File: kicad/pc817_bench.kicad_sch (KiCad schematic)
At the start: 14 parts, among them J1 24V inputs, J2 Arduino UNO R4, U1 PC817, U2 PC817

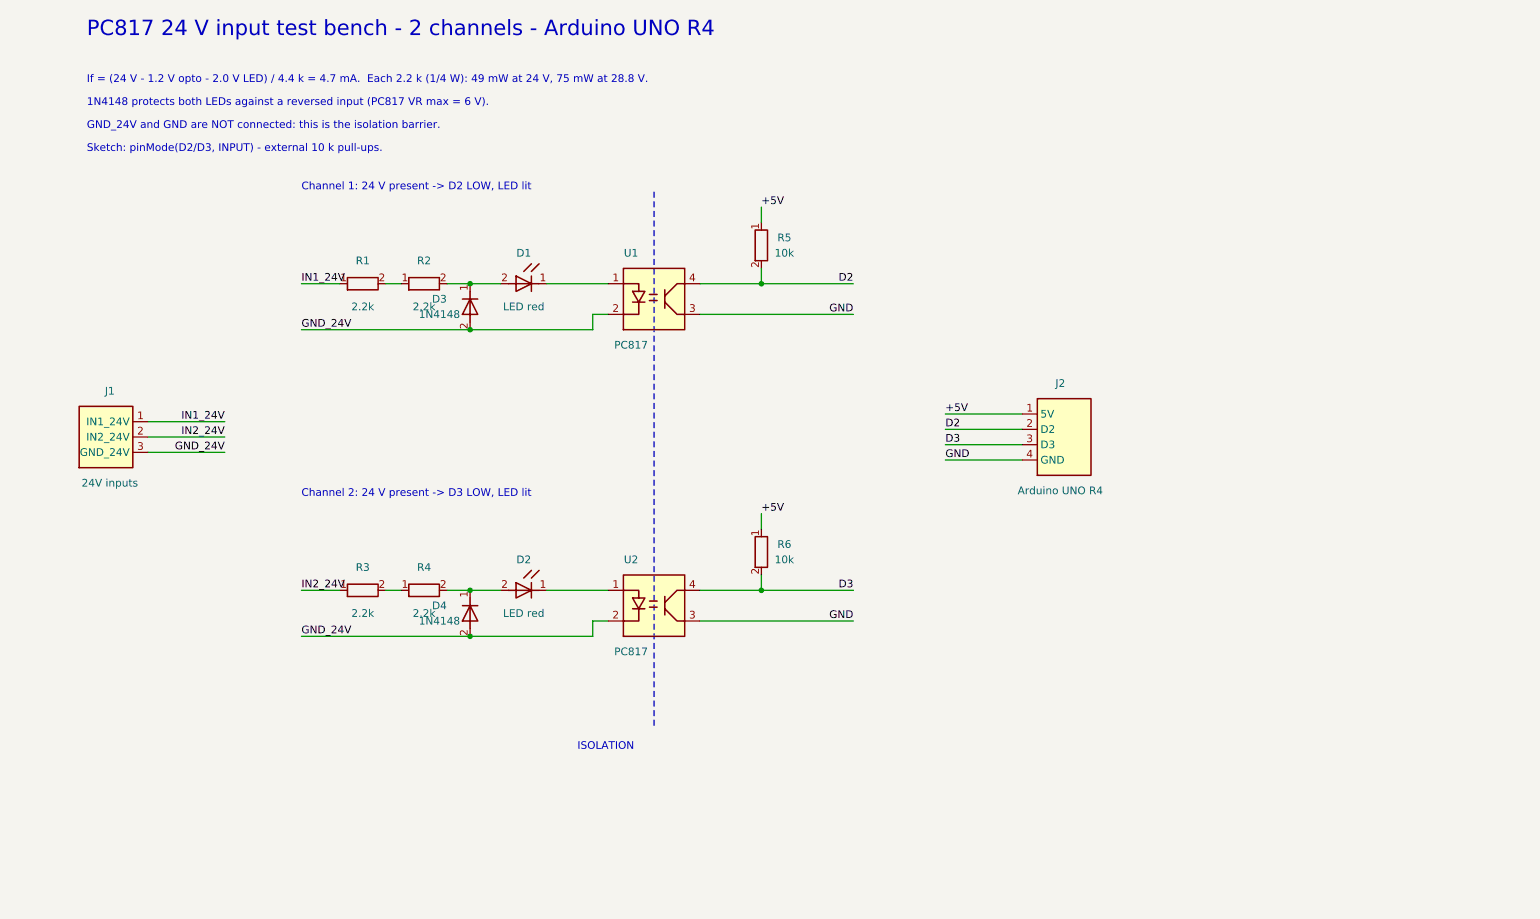
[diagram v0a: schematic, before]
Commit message: Draw the Arduino UNO R4 WiFi as a full header symbol instead of a 4-pin connector
Unused pins carry no-connect marks; all three GND pins join the GND net.
Rule check: 0 violations (KiCad 10.0.6).

Co-Authored-By: Claude Fable 5.1 <noreply@anthropic.com>
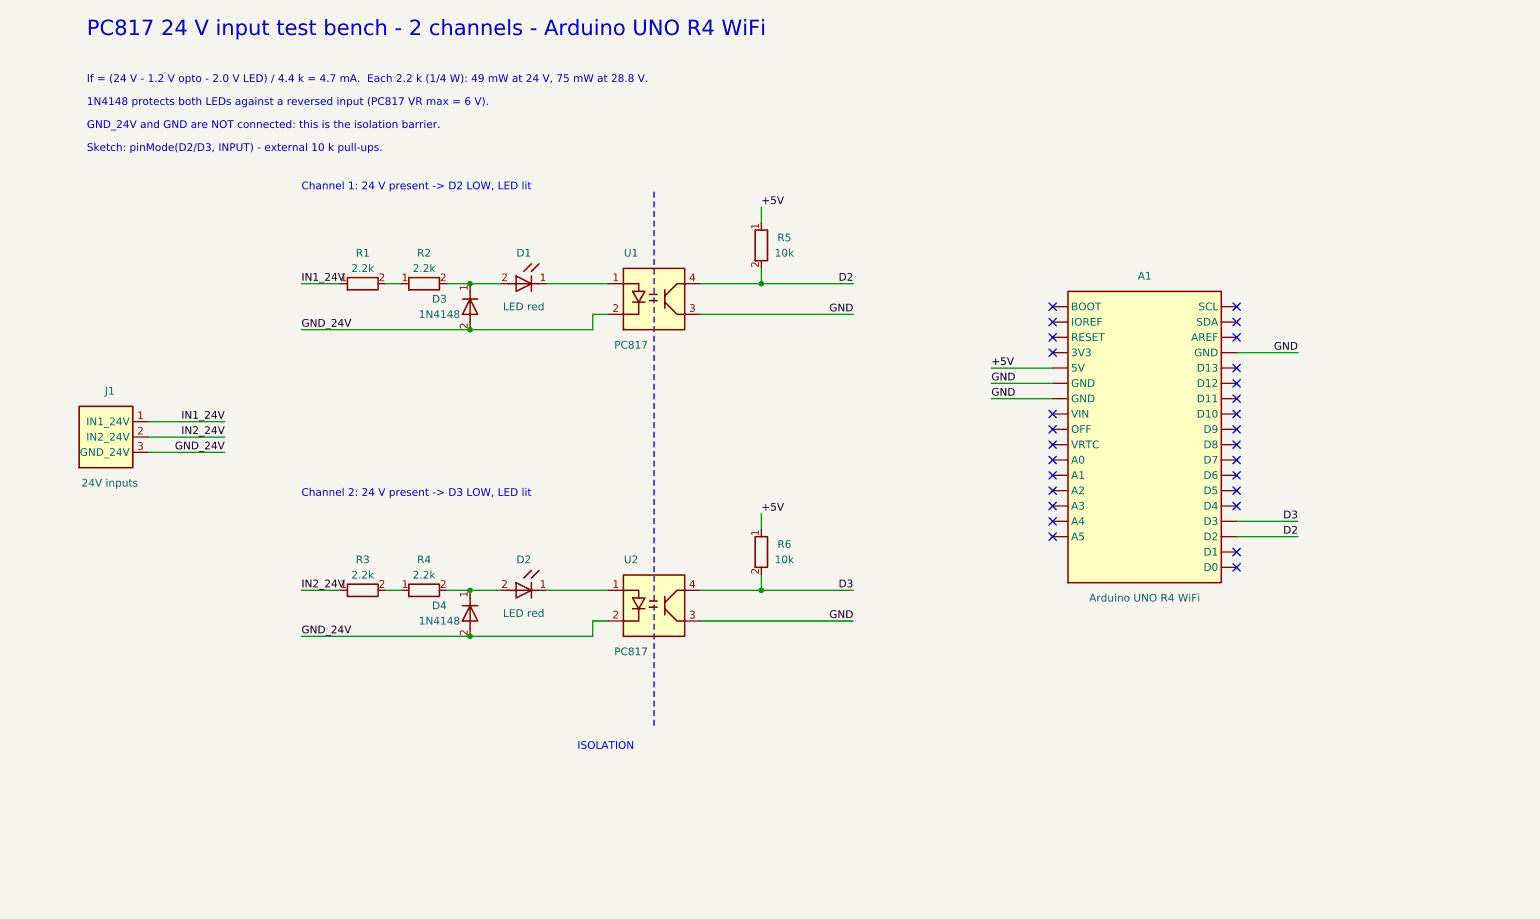
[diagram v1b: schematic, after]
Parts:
- removed J2: Arduino UNO R4, symbol bench:CONN4
- added A1: Arduino UNO R4 WiFi, symbol bench:UNO_R4_WIFI
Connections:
- net +5V: now also A1.5V
- net D2: now also A1.D2
- net D3: now also A1.D3
- net GND: now also A1.GND1 (GND), A1.GND2 (GND), A1.GND3 (GND)
- no-connect marks 0 -> 28
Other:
- note added: "PC817 24 V input test bench - 2 channels - Arduino UNO R4 WiFi"
- note removed: "PC817 24 V input test bench - 2 channels - Arduino UNO R4"
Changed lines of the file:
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@@
 (kicad_sch (version 20230121) (generator eeschema)
   (paper "A4")
-  (title_block (title "PC817 24 V input test bench") (date "2026-10-02") (rev "0.2")
+  (title_block (title "PC817 24 V input test bench") (date "2026-10-02") (rev "0.3")
     (comment 1 "Generated by generate.py - edit the script, not this file"))
   (symbol (lib_id "bench:R_H") (at 71.12 71.12 0) (unit 1) (in_bom yes) (on_board yes) (dnp no)
-    (property "Reference" "R1" (at 71.12 67.31 0) (effects (font (size 1.27 1.27))))
-    (property "Value" "2.2k" (at 71.12 74.93 0) (effects (font (size 1.27 1.27))))
+    (property "Reference" "R1" (at 71.12 66.04 0) (effects (font (size 1.27 1.27))))
+    (property "Value" "2.2k" (at 71.12 68.58 0) (effects (font (size 1.27 1.27))))
     (property "Footprint" "" (at 71.12 71.12 0) (effects (font (size 1.27 1.27)) hide))
     (property "Datasheet" "" (at 71.12 71.12 0) (effects (font (size 1.27 1.27)) hide))
@@
     (instances (project "pc817_bench" (path "/6f1d2c1e-0a4b-4c55-9a51-2b8f0c817001" (reference "R1") (unit 1)))))
   (symbol (lib_id "bench:R_H") (at 81.28 71.12 0) (unit 1) (in_bom yes) (on_board yes) (dnp no)
-    (property "Reference" "R2" (at 81.28 67.31 0) (effects (font (size 1.27 1.27))))
-    (property "Value" "2.2k" (at 81.28 74.93 0) (effects (font (size 1.27 1.27))))
+    (property "Reference" "R2" (at 81.28 66.04 0) (effects (font (size 1.27 1.27))))
+    (property "Value" "2.2k" (at 81.28 68.58 0) (effects (font (size 1.27 1.27))))
     (property "Footprint" "" (at 81.28 71.12 0) (effects (font (size 1.27 1.27)) hide))
     (property "Datasheet" "" (at 81.28 71.12 0) (effects (font (size 1.27 1.27)) hide))
@@
   (text "Channel 1: 24 V present -> D2 LOW, LED lit" (at 60.96 55.88 0) (effects (font (size 1.27 1.27)) (justify left bottom)))
   (symbol (lib_id "bench:R_H") (at 71.12 121.92 0) (unit 1) (in_bom yes) (on_board yes) (dnp no)
-    (property "Reference" "R3" (at 71.12 118.11 0) (effects (font (size 1.27 1.27))))
-    (property "Value" "2.2k" (at 71.12 125.73 0) (effects (font (size 1.27 1.27))))
+    (property "Reference" "R3" (at 71.12 116.84 0) (effects (font (size 1.27 1.27))))
+    (property "Value" "2.2k" (at 71.12 119.38 0) (effects (font (size 1.27 1.27))))
     (property "Footprint" "" (at 71.12 121.92 0) (effects (font (size 1.27 1.27)) hide))
     (property "Datasheet" "" (at 71.12 121.92 0) (effects (font (size 1.27 1.27)) hide))
@@
     (instances (project "pc817_bench" (path "/6f1d2c1e-0a4b-4c55-9a51-2b8f0c817001" (reference "R3") (unit 1)))))
   (symbol (lib_id "bench:R_H") (at 81.28 121.92 0) (unit 1) (in_bom yes) (on_board yes) (dnp no)
-    (property "Reference" "R4" (at 81.28 118.11 0) (effects (font (size 1.27 1.27))))
-    (property "Value" "2.2k" (at 81.28 125.73 0) (effects (font (size 1.27 1.27))))
+    (property "Reference" "R4" (at 81.28 116.84 0) (effects (font (size 1.27 1.27))))
+    (property "Value" "2.2k" (at 81.28 119.38 0) (effects (font (size 1.27 1.27))))
     (property "Footprint" "" (at 81.28 121.92 0) (effects (font (size 1.27 1.27)) hide))
     (property "Datasheet" "" (at 81.28 121.92 0) (effects (font (size 1.27 1.27)) hide))
@@
   (wire (pts (xy 35.56 99.06) (xy 48.26 99.06)) (stroke (width 0) (type default)))
   (label "GND_24V" (at 48.26 99.06 0) (effects (font (size 1.27 1.27)) (justify right bottom)))
-  (symbol (lib_id "bench:CONN4") (at 185.42 96.52 0) (unit 1) (in_bom yes) (on_board yes) (dnp no)
-    (property "Reference" "J2" (at 186.69 87.63 0) (effects (font (size 1.27 1.27))))
-    (property "Value" "Arduino UNO R4" (at 186.69 105.41 0) (effects (font (size 1.27 1.27))))
-    (property "Footprint" "" (at 185.42 96.52 0) (effects (font (size 1.27 1.27)) hide))
-    (property "Datasheet" "" (at 185.42 96.52 0) (effects (font (size 1.27 1.27)) hide))
-    (pin "1") (pin "2") (pin "3") (pin "4")
-    (instances (project "pc817_bench" (path "/6f1d2c1e-0a4b-4c55-9a51-2b8f0c817001" (reference "J2") (unit 1)))))
-  (wire (pts (xy 167.64 92.71) (xy 180.34 92.71)) (stroke (width 0) (type default)))
-  (label "+5V" (at 167.64 92.71 0) (effects (font (size 1.27 1.27)) (justify left bottom)))
-  (wire (pts (xy 167.64 95.25) (xy 180.34 95.25)) (stroke (width 0) (type default)))
-  (label "D2" (at 167.64 95.25 0) (effects (font (size 1.27 1.27)) (justify left bottom)))
-  (wire (pts (xy 167.64 97.79) (xy 180.34 97.79)) (stroke (width 0) (type default)))
-  (label "D3" (at 167.64 97.79 0) (effects (font (size 1.27 1.27)) (justify left bottom)))
-  (wire (pts (xy 167.64 100.33) (xy 180.34 100.33)) (stroke (width 0) (type default)))
-  (label "GND" (at 167.64 100.33 0) (effects (font (size 1.27 1.27)) (justify left bottom)))
-  (text "PC817 24 V input test bench - 2 channels - Arduino UNO R4" (at 25.4 30.48 0) (effects (font (size 2.54 2.54)) (justify left bottom)))
+  (symbol (lib_id "bench:UNO_R4_WIFI") (at 200.66 96.52 0) (unit 1) (in_bom yes) (on_board yes) (dnp no)
+    (property "Reference" "A1" (at 200.66 69.85 0) (effects (font (size 1.27 1.27))))
+    (property "Value" "Arduino UNO R4 WiFi" (at 200.66 123.19 0) (effects (font (size 1.27 1.27))))
+    (property "Footprint" "" (at 200.66 96.52 0) (effects (font (size 1.27 1.27)) hide))
+    (property "Datasheet" "" (at 200.66 96.52 0) (effects (font (size 1.27 1.27)) hide))
+    (pin "BOOT") (pin "IOREF") (pin "RESET") (pin "3V3") (pin "5V") (pin "GND1") (pin "GND2") (pin "VIN") (pin "OFF") (pin "VRTC") (pin "A0") (pin "A1") (pin "A2") (pin "A3") (pin "A4") (pin "A5") (pin "SCL") (pin "SDA") (pin "AREF") (pin "GND3") (pin "D13") (pin "D12") (pin "D11") (pin "D10") (pin "D9") (pin "D8") (pin "D7") (pin "D6") (pin "D5") (pin "D4") (pin "D3") (pin "D2") (pin "D1") (pin "D0")
+    (instances (project "pc817_bench" (path "/6f1d2c1e-0a4b-4c55-9a51-2b8f0c817001" (reference "A1") (unit 1)))))
+  (no_connect (at 185.42 74.93))
+  (no_connect (at 185.42 77.47))
+  (no_connect (at 185.42 80.01))
+  (no_connect (at 185.42 82.55))
+  (wire (pts (xy 185.42 85.09) (xy 175.26 85.09)) (stroke (width 0) (type default)))
+  (label "+5V" (at 175.26 85.09 0) (effects (font (size 1.27 1.27)) (justify left bottom)))
+  (wire (pts (xy 185.42 87.63) (xy 175.26 87.63)) (stroke (width 0) (type default)))
+  (label "GND" (at 175.26 87.63 0) (effects (font (size 1.27 1.27)) (justify left bottom)))
+  (wire (pts (xy 185.42 90.17) (xy 175.26 90.17)) (stroke (width 0) (type default)))
+  (label "GND" (at 175.26 90.17 0) (effects (font (size 1.27 1.27)) (justify left bottom)))
+  (no_connect (at 185.42 92.71))
+  (no_connect (at 185.42 95.25))
+  (no_connect (at 185.42 97.79))
+  (no_connect (at 185.42 100.33))
+  (no_connect (at 185.42 102.87))
+  (no_connect (at 185.42 105.41))
+  (no_connect (at 185.42 107.95))
+  (no_connect (at 185.42 110.49))
+  (no_connect (at 185.42 113.03))
+  (no_connect (at 215.9 74.93))
+  (no_connect (at 215.9 77.47))
+  (no_connect (at 215.9 80.01))
+  (wire (pts (xy 215.9 82.55) (xy 226.06 82.55)) (stroke (width 0) (type default)))
+  (label "GND" (at 226.06 82.55 0) (effects (font (size 1.27 1.27)) (justify right bottom)))
+  (no_connect (at 215.9 85.09))
+  (no_connect (at 215.9 87.63))
+  (no_connect (at 215.9 90.17))
+  (no_connect (at 215.9 92.71))
+  (no_connect (at 215.9 95.25))
+  (no_connect (at 215.9 97.79))
+  (no_connect (at 215.9 100.33))
+  (no_connect (at 215.9 102.87))
+  (no_connect (at 215.9 105.41))
+  (no_connect (at 215.9 107.95))
+  (wire (pts (xy 215.9 110.49) (xy 226.06 110.49)) (stroke (width 0) (type default)))
+  (label "D3" (at 226.06 110.49 0) (effects (font (size 1.27 1.27)) (justify right bottom)))
+  (wire (pts (xy 215.9 113.03) (xy 226.06 113.03)) (stroke (width 0) (type default)))
+  (label "D2" (at 226.06 113.03 0) (effects (font (size 1.27 1.27)) (justify right bottom)))
+  (no_connect (at 215.9 115.57))
+  (no_connect (at 215.9 118.11))
+  (text "PC817 24 V input test bench - 2 channels - Arduino UNO R4 WiFi" (at 25.4 30.48 0) (effects (font (size 2.54 2.54)) (justify left bottom)))
   (text "If = (24 V - 1.2 V opto - 2.0 V LED) / 4.4 k = 4.7 mA.  Each 2.2 k (1/4 W): 49 mW at 24 V, 75 mW at 28.8 V." (at 25.4 38.1 0) (effects (font (size 1.27 1.27)) (justify left bottom)))
   (text "1N4148 protects both LEDs against a reversed input (PC817 VR max = 6 V)." (at 25.4 41.91 0) (effects (font (size 1.27 1.27)) (justify left bottom)))

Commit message: Pull-ups to IOREF so the bench works on both UNO R4 WiFi (5 V) and UNO Q (3.3 V)
The Arduino symbol is now the standard UNO shield header only.

Co-Authored-By: Claude Fable 5.1 <noreply@anthropic.com>
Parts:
- A1: value Arduino UNO R4 WiFi -> UNO R4 WiFi or UNO Q
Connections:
- net IOREF: now reaches A1.IOREF
- net IOREF: now also R5.1, R6.1
- removed net +5V: A1.5V, R5.1, R6.1
- no-connect marks 28 -> 26
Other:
- note added: "PC817 24 V input test bench - 2 channels - shield for Arduino UNO R4 WiFi / UNO Q"
- note added: "Pull-ups go to IOREF: 5 V on the UNO R4 WiFi, 3.3 V on the UNO Q. Never to the 5V pin. Sketch: pinMode(D2/D3, INPUT)."
- note removed: "PC817 24 V input test bench - 2 channels - Arduino UNO R4 WiFi"
- note removed: "Sketch: pinMode(D2/D3, INPUT) - external 10 k pull-ups."
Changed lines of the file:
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@@
 (kicad_sch (version 20230121) (generator eeschema)
   (paper "A4")
-  (title_block (title "PC817 24 V input test bench") (date "2026-10-02") (rev "0.3")
+  (title_block (title "PC817 24 V input test bench") (date "2026-10-02") (rev "0.4")
     (comment 1 "Generated by generate.py - edit the script, not this file"))
   (symbol (lib_id "bench:R_H") (at 71.12 71.12 0) (unit 1) (in_bom yes) (on_board yes) (dnp no)
@@
   (wire (pts (xy 137.16 68.58) (xy 137.16 71.12)) (stroke (width 0) (type default)))
   (wire (pts (xy 137.16 60.96) (xy 137.16 58.42)) (stroke (width 0) (type default)))
-  (label "+5V" (at 137.16 58.42 0) (effects (font (size 1.27 1.27)) (justify left bottom)))
+  (label "IOREF" (at 137.16 58.42 0) (effects (font (size 1.27 1.27)) (justify left bottom)))
   (wire (pts (xy 127 76.2) (xy 152.4 76.2)) (stroke (width 0) (type default)))
   (label "GND" (at 152.4 76.2 0) (effects (font (size 1.27 1.27)) (justify right bottom)))
@@
   (wire (pts (xy 137.16 119.38) (xy 137.16 121.92)) (stroke (width 0) (type default)))
   (wire (pts (xy 137.16 111.76) (xy 137.16 109.22)) (stroke (width 0) (type default)))
-  (label "+5V" (at 137.16 109.22 0) (effects (font (size 1.27 1.27)) (justify left bottom)))
+  (label "IOREF" (at 137.16 109.22 0) (effects (font (size 1.27 1.27)) (justify left bottom)))
   (wire (pts (xy 127 127) (xy 152.4 127)) (stroke (width 0) (type default)))
   (label "GND" (at 152.4 127 0) (effects (font (size 1.27 1.27)) (justify right bottom)))
@@
   (symbol (lib_id "bench:UNO_R4_WIFI") (at 200.66 96.52 0) (unit 1) (in_bom yes) (on_board yes) (dnp no)
     (property "Reference" "A1" (at 200.66 69.85 0) (effects (font (size 1.27 1.27))))
-    (property "Value" "Arduino UNO R4 WiFi" (at 200.66 123.19 0) (effects (font (size 1.27 1.27))))
+    (property "Value" "UNO R4 WiFi or UNO Q" (at 200.66 123.19 0) (effects (font (size 1.27 1.27))))
     (property "Footprint" "" (at 200.66 96.52 0) (effects (font (size 1.27 1.27)) hide))
     (property "Datasheet" "" (at 200.66 96.52 0) (effects (font (size 1.27 1.27)) hide))
-    (pin "BOOT") (pin "IOREF") (pin "RESET") (pin "3V3") (pin "5V") (pin "GND1") (pin "GND2") (pin "VIN") (pin "OFF") (pin "VRTC") (pin "A0") (pin "A1") (pin "A2") (pin "A3") (pin "A4") (pin "A5") (pin "SCL") (pin "SDA") (pin "AREF") (pin "GND3") (pin "D13") (pin "D12") (pin "D11") (pin "D10") (pin "D9") (pin "D8") (pin "D7") (pin "D6") (pin "D5") (pin "D4") (pin "D3") (pin "D2") (pin "D1") (pin "D0")
+    (pin "NC") (pin "IOREF") (pin "RESET") (pin "3V3") (pin "5V") (pin "GND1") (pin "GND2") (pin "VIN") (pin "A0") (pin "A1") (pin "A2") (pin "A3") (pin "A4") (pin "A5") (pin "SCL") (pin "SDA") (pin "AREF") (pin "GND3") (pin "D13") (pin "D12") (pin "D11") (pin "D10") (pin "D9") (pin "D8") (pin "D7") (pin "D6") (pin "D5") (pin "D4") (pin "D3") (pin "D2") (pin "D1") (pin "D0")
     (instances (project "pc817_bench" (path "/6f1d2c1e-0a4b-4c55-9a51-2b8f0c817001" (reference "A1") (unit 1)))))
   (no_connect (at 185.42 74.93))
-  (no_connect (at 185.42 77.47))
+  (wire (pts (xy 185.42 77.47) (xy 175.26 77.47)) (stroke (width 0) (type default)))
+  (label "IOREF" (at 175.26 77.47 0) (effects (font (size 1.27 1.27)) (justify left bottom)))
   (no_connect (at 185.42 80.01))
   (no_connect (at 185.42 82.55))
-  (wire (pts (xy 185.42 85.09) (xy 175.26 85.09)) (stroke (width 0) (type default)))
-  (label "+5V" (at 175.26 85.09 0) (effects (font (size 1.27 1.27)) (justify left bottom)))
+  (no_connect (at 185.42 85.09))
   (wire (pts (xy 185.42 87.63) (xy 175.26 87.63)) (stroke (width 0) (type default)))
   (label "GND" (at 175.26 87.63 0) (effects (font (size 1.27 1.27)) (justify left bottom)))
@@
   (no_connect (at 185.42 105.41))
   (no_connect (at 185.42 107.95))
-  (no_connect (at 185.42 110.49))
-  (no_connect (at 185.42 113.03))
   (no_connect (at 215.9 74.93))
   (no_connect (at 215.9 77.47))
@@
   (no_connect (at 215.9 115.57))
   (no_connect (at 215.9 118.11))
-  (text "PC817 24 V input test bench - 2 channels - Arduino UNO R4 WiFi" (at 25.4 30.48 0) (effects (font (size 2.54 2.54)) (justify left bottom)))
+  (text "PC817 24 V input test bench - 2 channels - shield for Arduino UNO R4 WiFi / UNO Q" (at 25.4 30.48 0) (effects (font (size 2.54 2.54)) (justify left bottom)))
   (text "If = (24 V - 1.2 V opto - 2.0 V LED) / 4.4 k = 4.7 mA.  Each 2.2 k (1/4 W): 49 mW at 24 V, 75 mW at 28.8 V." (at 25.4 38.1 0) (effects (font (size 1.27 1.27)) (justify left bottom)))
   (text "1N4148 protects both LEDs against a reversed input (PC817 VR max = 6 V)." (at 25.4 41.91 0) (effects (font (size 1.27 1.27)) (justify left bottom)))
   (text "GND_24V and GND are NOT connected: this is the isolation barrier." (at 25.4 45.72 0) (effects (font (size 1.27 1.27)) (justify left bottom)))
-  (text "Sketch: pinMode(D2/D3, INPUT) - external 10 k pull-ups." (at 25.4 49.53 0) (effects (font (size 1.27 1.27)) (justify left bottom)))
+  (text "Pull-ups go to IOREF: 5 V on the UNO R4 WiFi, 3.3 V on the UNO Q. Never to the 5V pin. Sketch: pinMode(D2/D3, INPUT)." (at 25.4 49.53 0) (effects (font (size 1.27 1.27)) (justify left bottom)))
   (text "ISOLATION" (at 106.68 148.59 0) (effects (font (size 1.27 1.27)) (justify left bottom)))
   (polyline (pts (xy 119.38 55.88) (xy 119.38 144.78)) (stroke (width 0.2) (type dash)))
